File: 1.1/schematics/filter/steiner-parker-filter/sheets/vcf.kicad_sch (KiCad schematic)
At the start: 68 parts, among them J2 Conn_01x05_Male, Q1 BC547B, Q2 BC547B, U1 TL072, U2 TL074

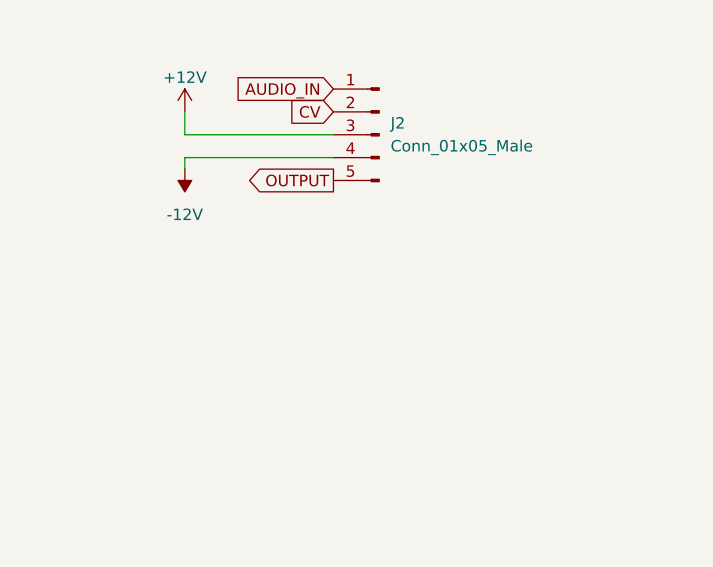
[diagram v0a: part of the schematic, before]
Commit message: Updated envelope UI and filter
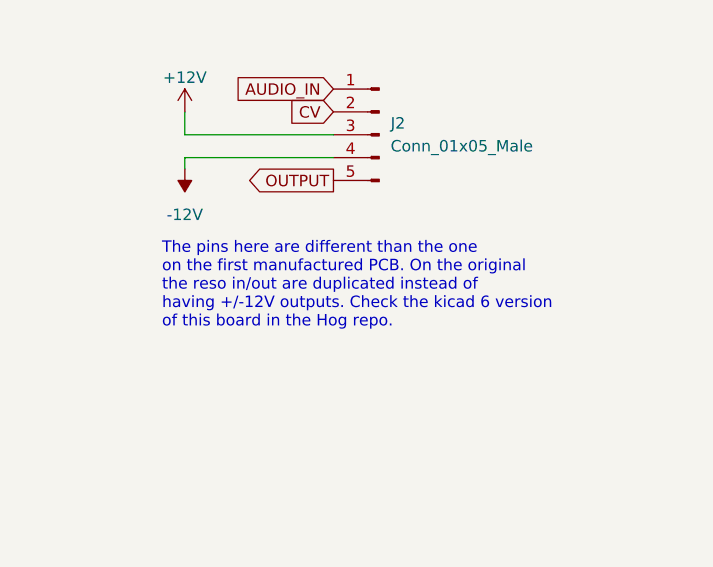
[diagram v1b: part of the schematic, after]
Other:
- note added: "The pins here are different than the one on the first manufactured PCB. On the original the reso in/out are duplicated instead of having +/-12V outputs. Check the kicad 6 version of this board in the Hog repo."
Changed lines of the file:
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@@
+    (effects (font (size 1.27 1.27)) (justify left bottom))
+  )
+  (text "The pins here are different than the one\non the first manufactured PCB. On the original\nthe reso in/out are duplicated instead of \nhaving +/-12V outputs. Check the kicad 6 version\nof this board in the Hog repo."
+    (at 290.83 157.48 0)
     (effects (font (size 1.27 1.27)) (justify left bottom))
   )
